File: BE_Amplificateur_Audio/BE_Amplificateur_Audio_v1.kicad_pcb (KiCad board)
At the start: 2 copper layers, 110 x 100 mm, 52 parts, among them J2 Conn_01x02, J3 Conn_01x03, Q1 2N2907, Q10 TIP32, Q11 BD138, Q12 TIP31, Q13 2N2222, Q2 2N2907, Q3 2N2907, Q4 2N2222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

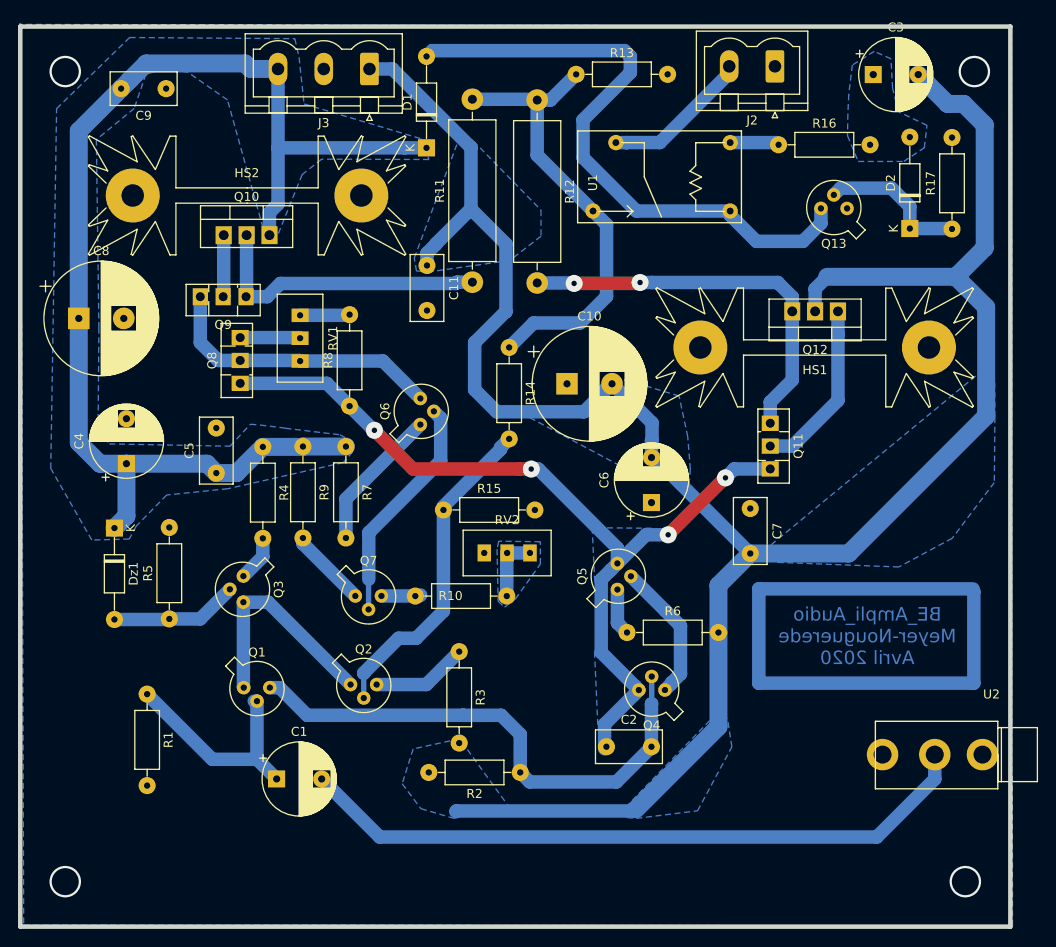
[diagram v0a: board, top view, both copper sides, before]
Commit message: Placement + Routage
Placement + routage (v0 à v2)
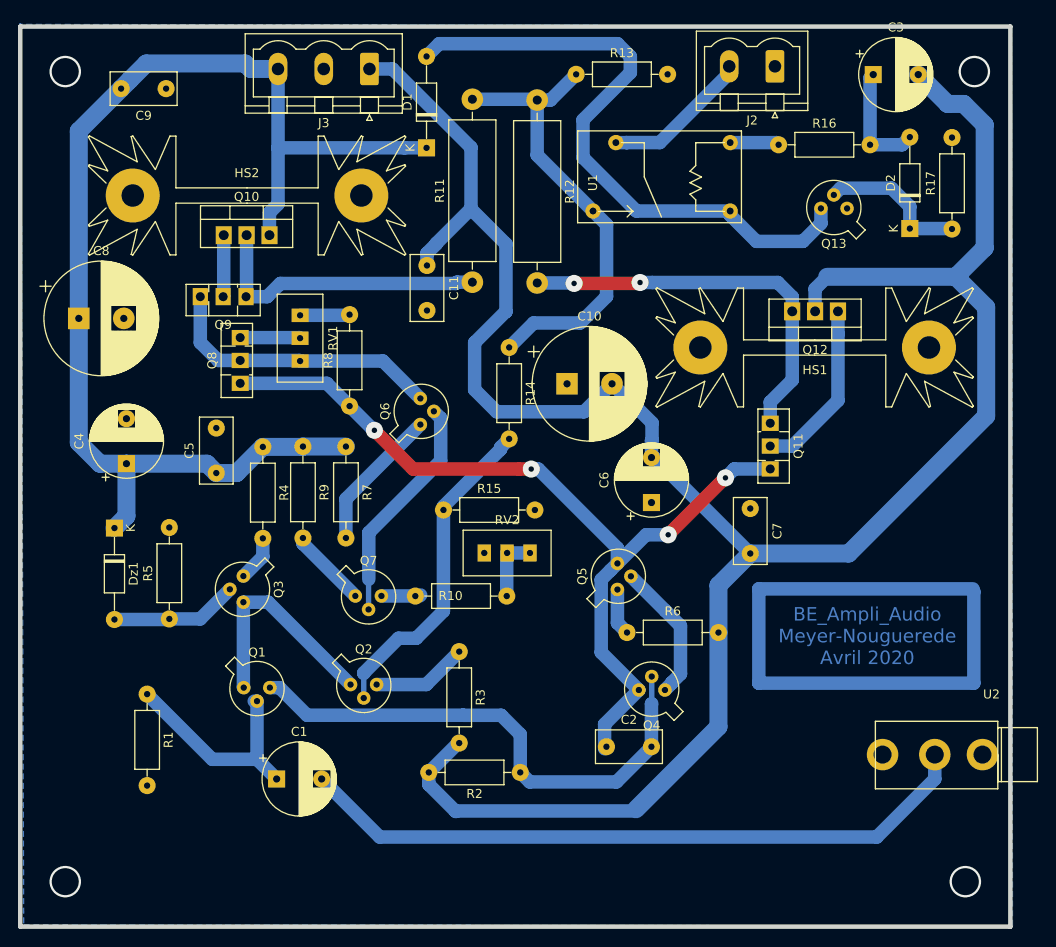
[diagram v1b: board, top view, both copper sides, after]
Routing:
- net Net-(C3-Pad1): track 0.04 -> 12.8 mm
- net -12V: track 246.0 -> 256.3 mm
- net Net-(D1-Pad2): track 69.6 -> 70.3 mm
- removed copper zone on B.Cu, net +12V
- removed copper zone on B.Cu, net -12V
- removed copper zone on B.Cu, net Net-(C2-Pad1)
- removed copper zone on B.Cu, net Net-(C3-Pad1)
- removed copper zone on B.Cu, net Net-(R10-Pad2)
